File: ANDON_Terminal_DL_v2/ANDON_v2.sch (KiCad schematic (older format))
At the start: 41 parts, among them P1 CONN_4, P10 CONN_1, P11 CONN_1, P12 CONN_1, P15 CONN_5X2, P2 PRG_CONN, P4 CONN_5, P5 CONN_8, P8 CONN_4, P9 CONN_1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

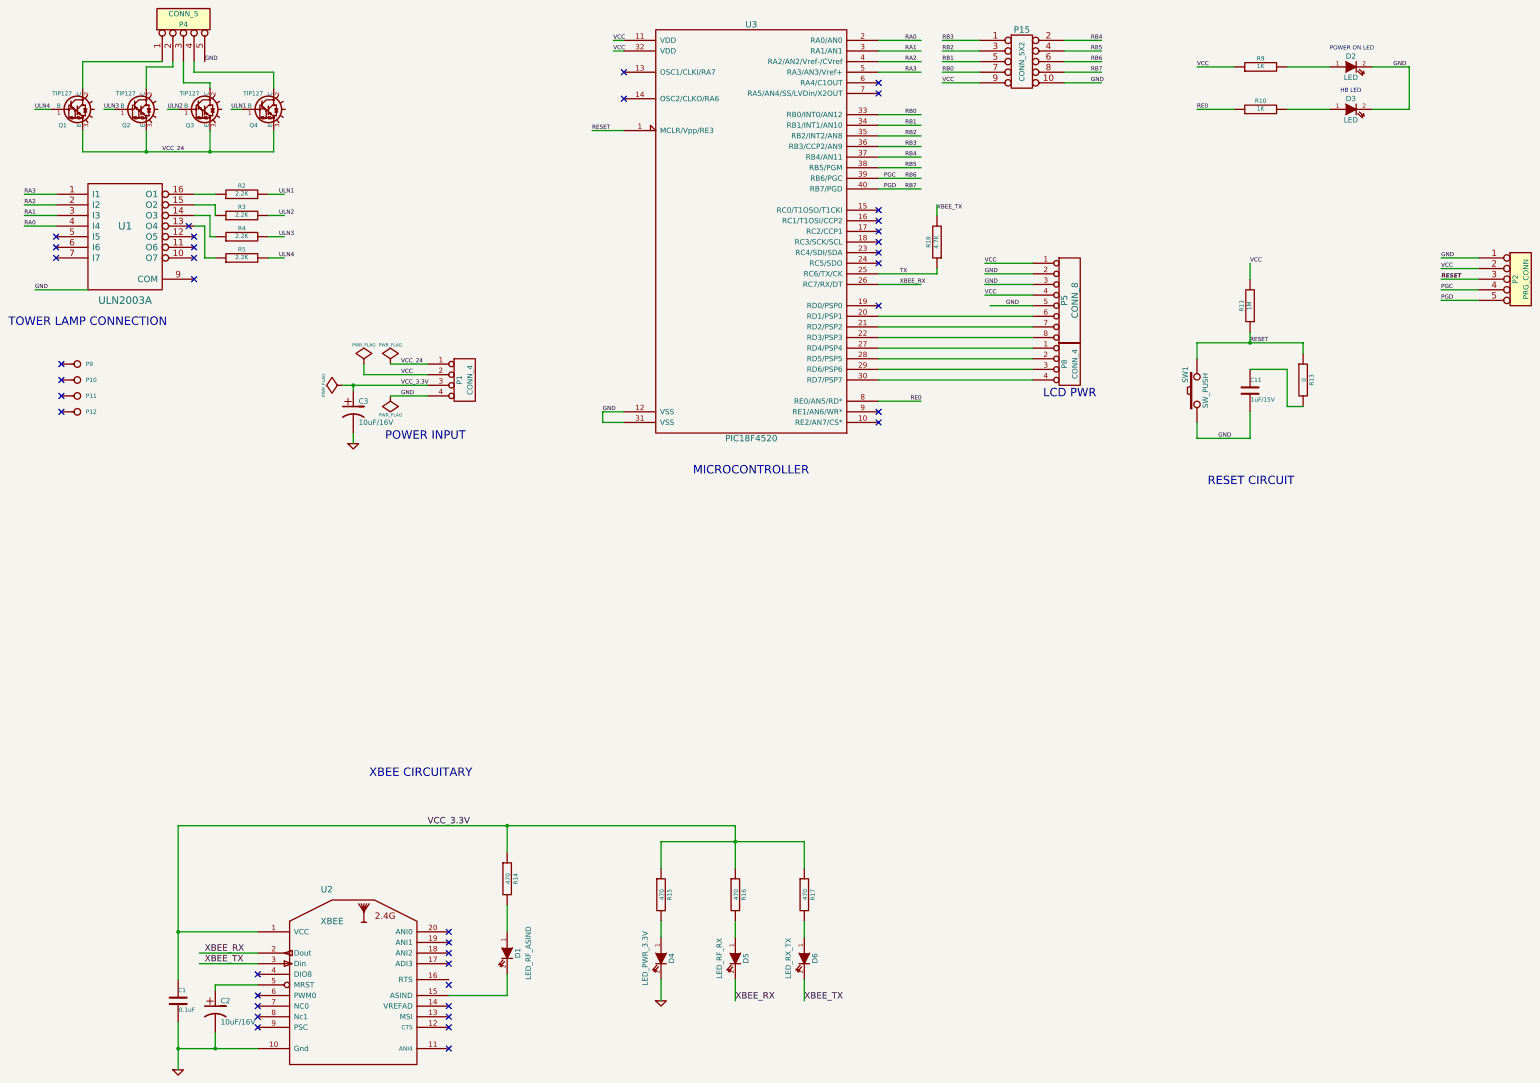
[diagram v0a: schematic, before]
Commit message: PIC PROGRAMMING CONNECTOR MODIFICATION
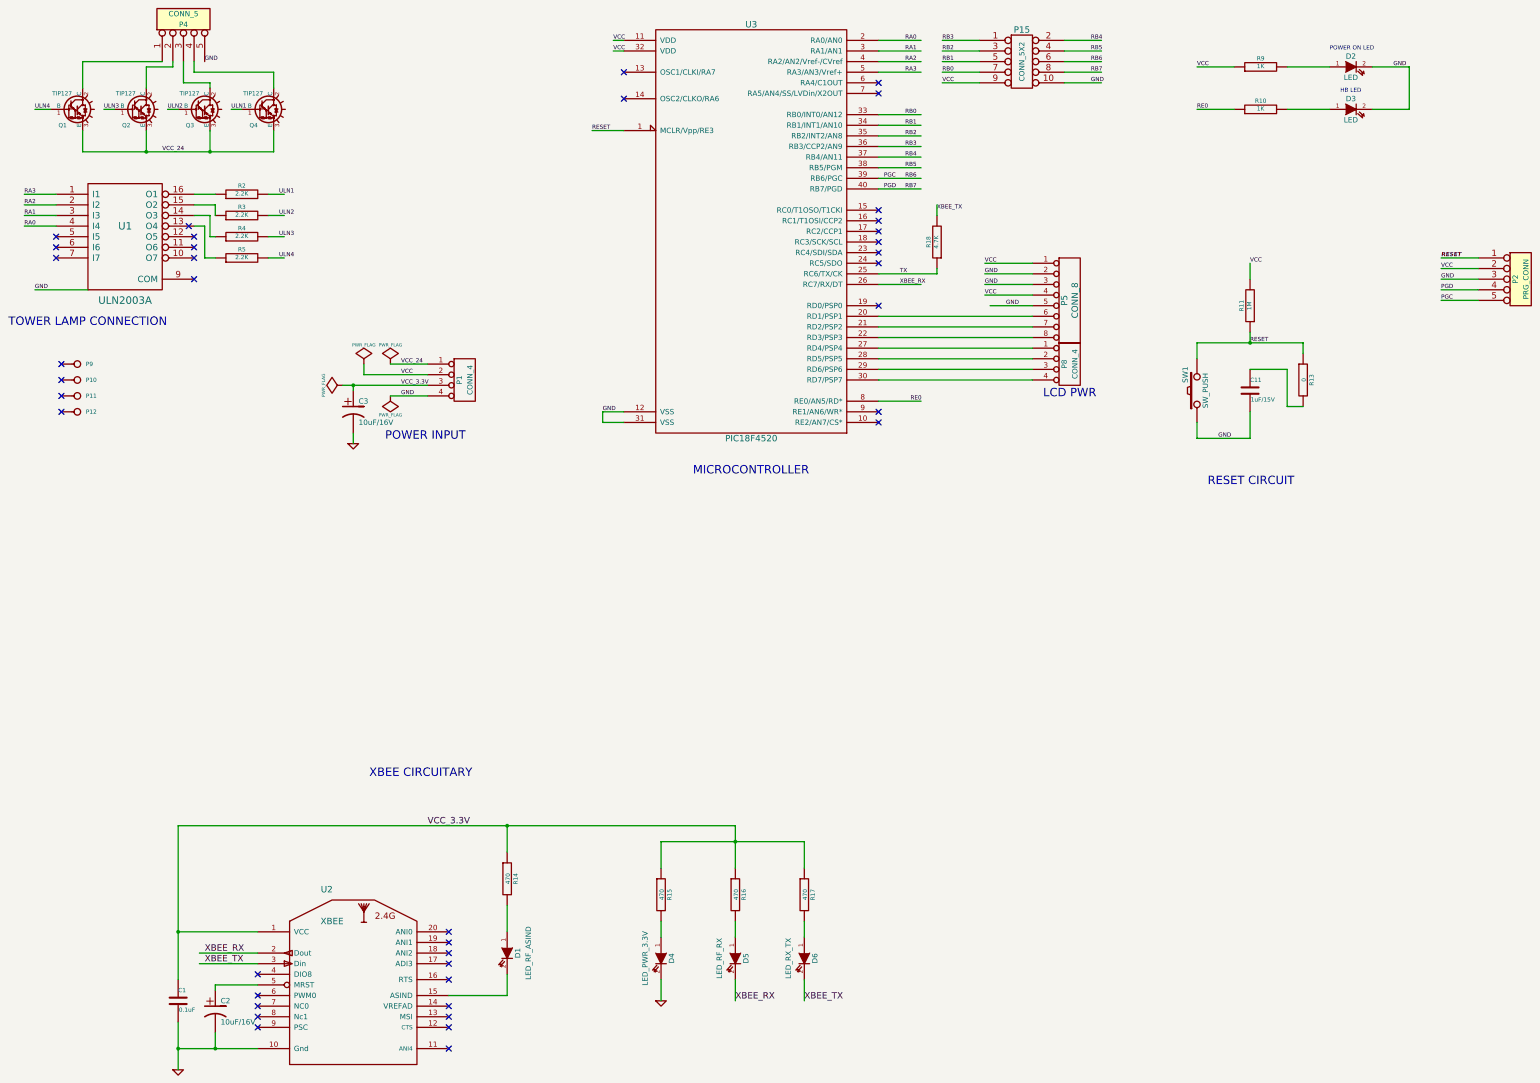
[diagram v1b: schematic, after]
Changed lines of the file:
@@
 Sheet 1 1
 Title ""
-Date "1 jul 2014"
+Date "15 aug 2016"
 Rev ""
 Comp ""
@@
 	1    0    0    -1
 $EndComp
-Text Label 14550 2950 0    39   ~ 0
+Text Label 14550 3150 0    39   ~ 0
 GND
 Text Label 14550 3050 0    39   ~ 0
 VCC
 Text Label 14550 3250 0    39   ~ 0
+PGD
+Text Label 14550 3350 0    39   ~ 0
 PGC
-Text Label 14550 3350 0    39   ~ 0
-PGD
 Text Label 2500 1950 0    39   ~ 0
 VCC_24
@@
 NoConn ~ 5200 10100
 NoConn ~ 5200 10000
-NoConn ~ 5200 9800
+NoConn ~ 5200 9750
 NoConn ~ 5200 9600
 NoConn ~ 5200 9500
@@
 Wire Wire Line
 	9800 2550 9800 2450
-Text Label 14550 3150 0    39   Italic 8
+Text Label 14550 2950 0    39   Italic 8
 RESET
 $Comp
